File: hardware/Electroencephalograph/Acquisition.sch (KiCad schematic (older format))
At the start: 59 parts, among them U1 ADS1298IPAG, U2 OPA330xxD

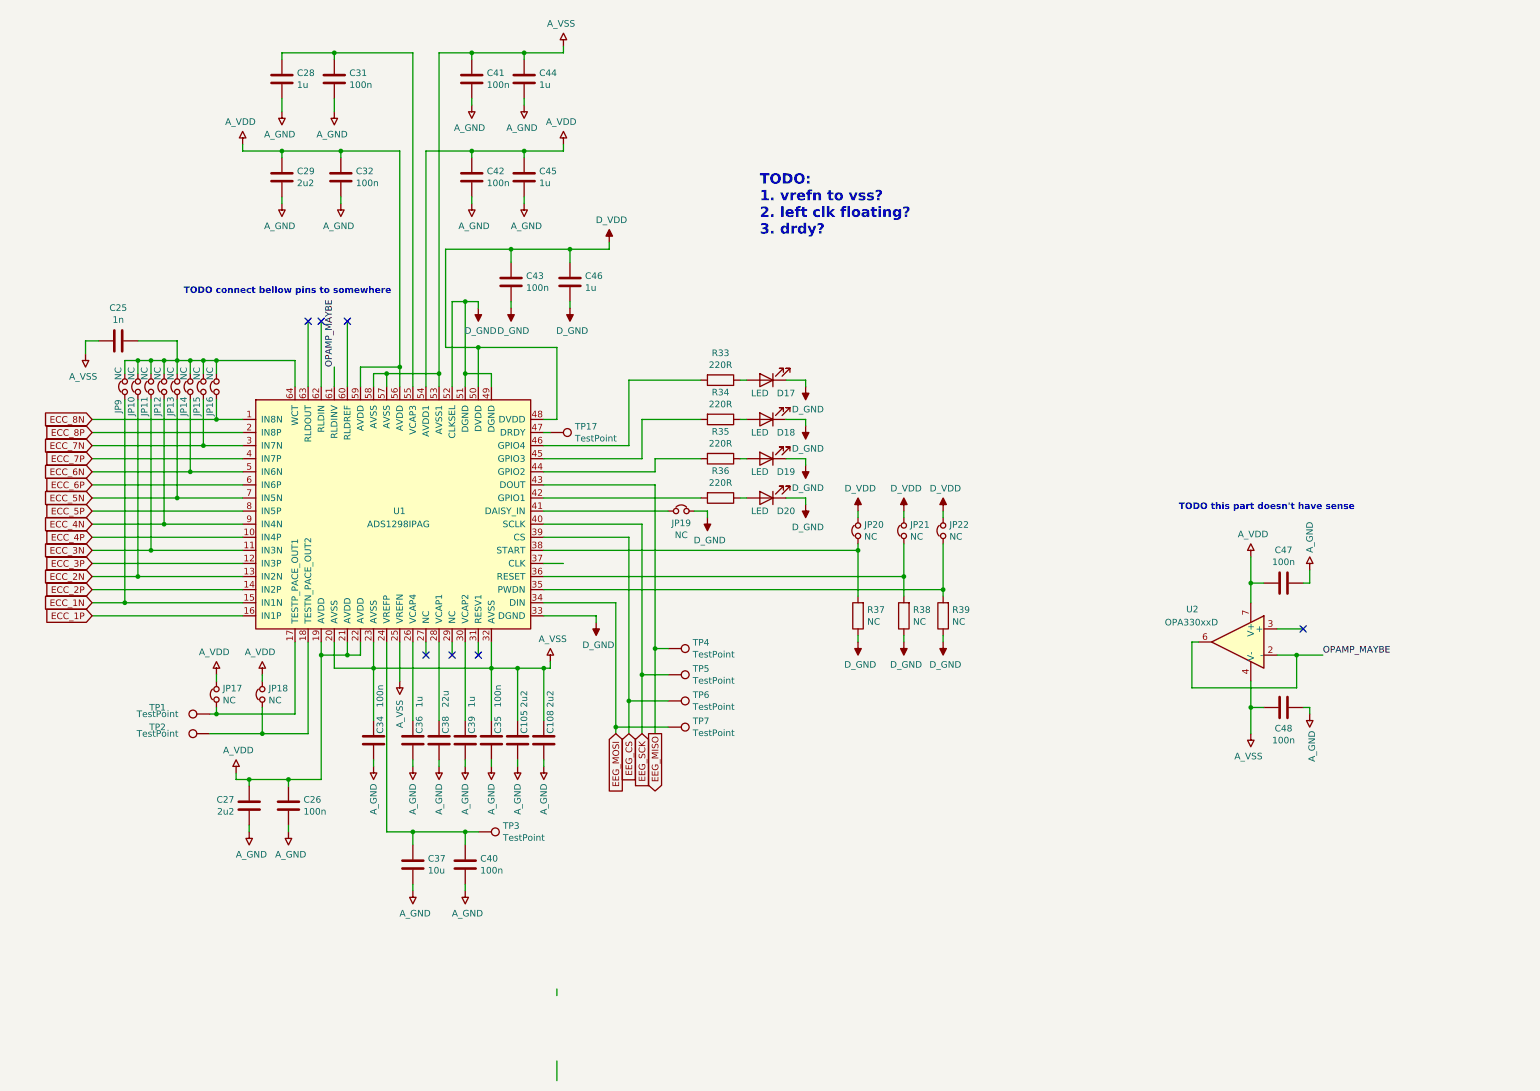
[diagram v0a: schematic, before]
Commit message: split user interface to separate sheets
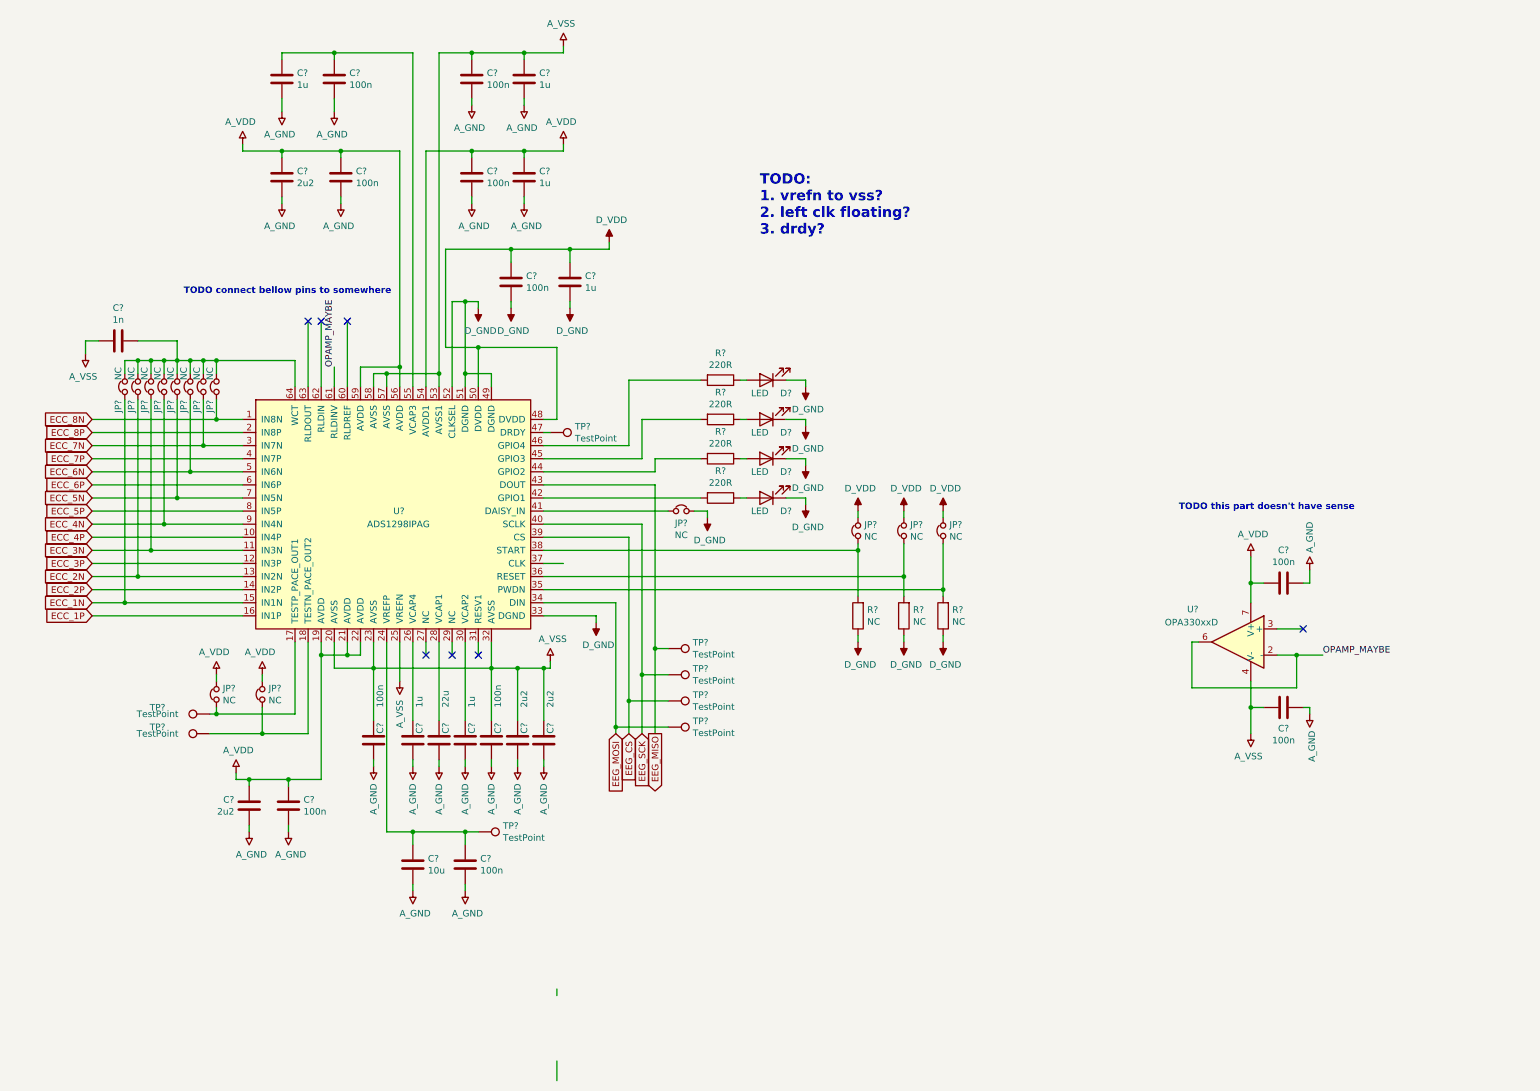
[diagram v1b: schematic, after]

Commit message: fix esp circuit
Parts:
- renumbered TP7 to TP17, TP17 to TP4, TP4 to TP5, TP5 to TP6, TP6 to TP7

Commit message: draft of mcu routing
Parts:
- D17, D18, D19, D20: footprint LED_SMD:LED_0603_1608Metric -> LED_SMD:LED_0402_1005Metric
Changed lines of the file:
@@
 F 0 "D20" H 6050 4300 50  0000 C CNN
 F 1 "LED" H 6250 4300 50  0000 C CNN
-F 2 "LED_SMD:LED_0603_1608Metric" H 6200 4200 50  0001 C CNN
+F 2 "LED_SMD:LED_0402_1005Metric" H 6200 4200 50  0001 C CNN
 F 3 "~" H 6200 4200 50  0001 C CNN
 	1    6200 4200
@@
 F 0 "D17" H 6050 3400 50  0000 C CNN
 F 1 "LED" H 6250 3400 50  0000 C CNN
-F 2 "LED_SMD:LED_0603_1608Metric" H 6200 3300 50  0001 C CNN
+F 2 "LED_SMD:LED_0402_1005Metric" H 6200 3300 50  0001 C CNN
 F 3 "~" H 6200 3300 50  0001 C CNN
 	1    6200 3300
@@
 F 0 "D18" H 6050 3700 50  0000 C CNN
 F 1 "LED" H 6250 3700 50  0000 C CNN
-F 2 "LED_SMD:LED_0603_1608Metric" H 6200 3600 50  0001 C CNN
+F 2 "LED_SMD:LED_0402_1005Metric" H 6200 3600 50  0001 C CNN
 F 3 "~" H 6200 3600 50  0001 C CNN
 	1    6200 3600
@@
 F 0 "D19" H 6050 4000 50  0000 C CNN
 F 1 "LED" H 6250 4000 50  0000 C CNN
-F 2 "LED_SMD:LED_0603_1608Metric" H 6200 3900 50  0001 C CNN
+F 2 "LED_SMD:LED_0402_1005Metric" H 6200 3900 50  0001 C CNN
 F 3 "~" H 6200 3900 50  0001 C CNN
 	1    6200 3900

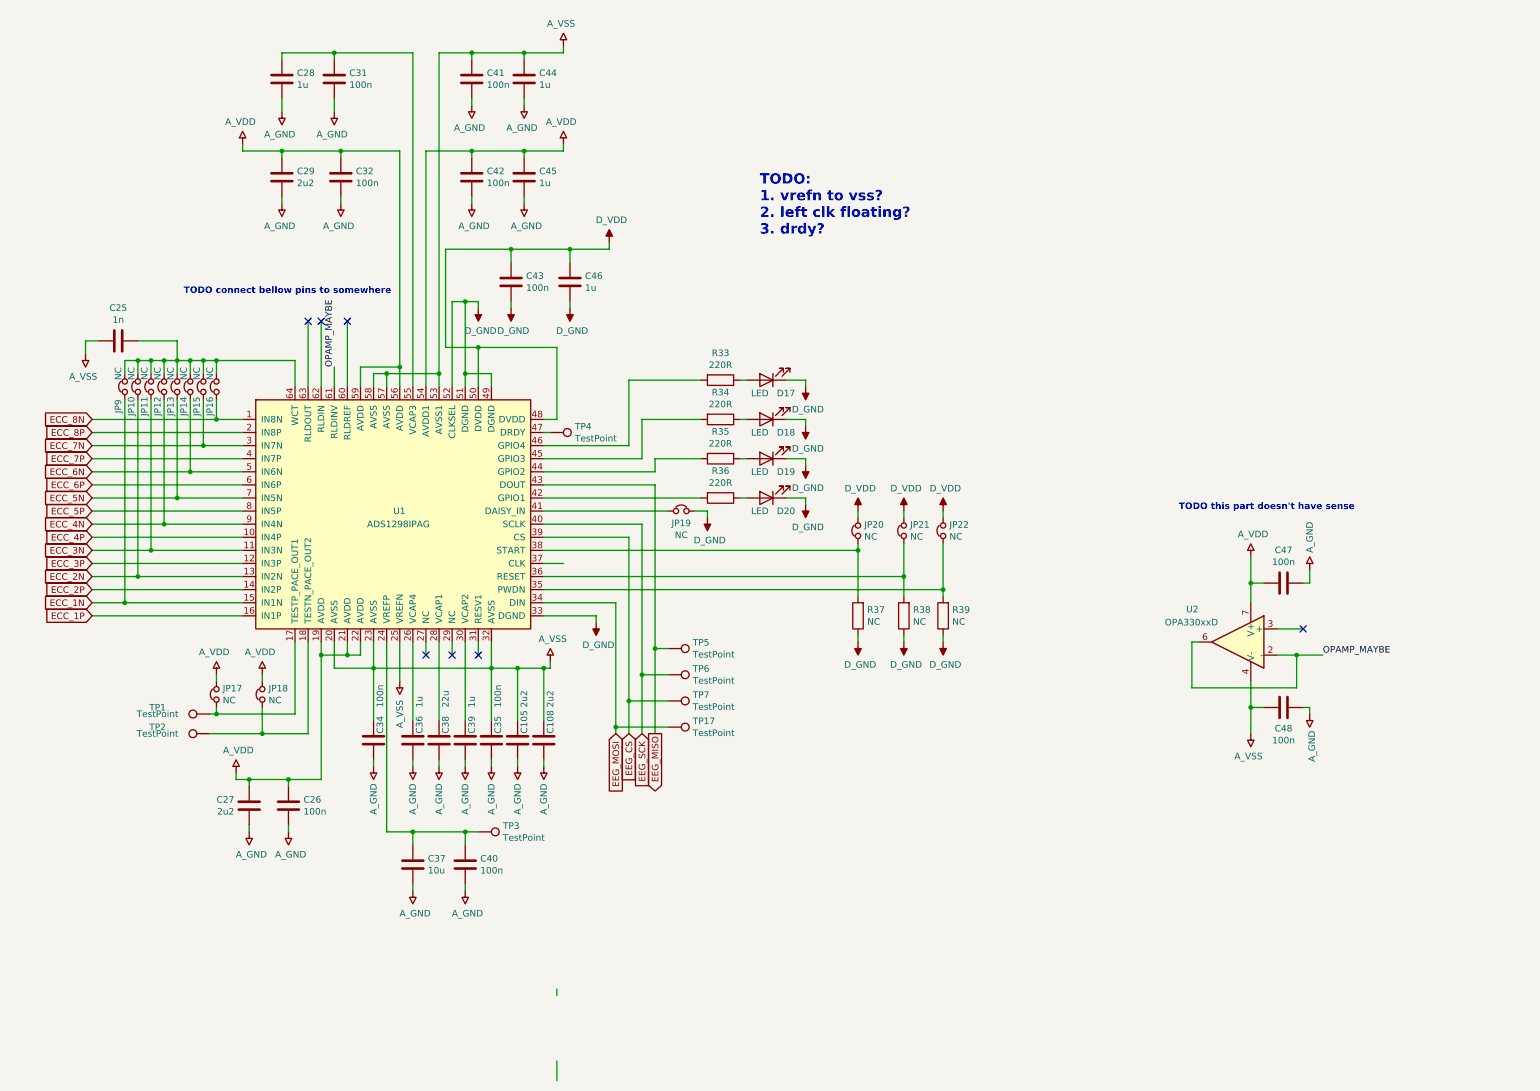
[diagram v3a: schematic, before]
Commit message: add right leg signal, update REDME
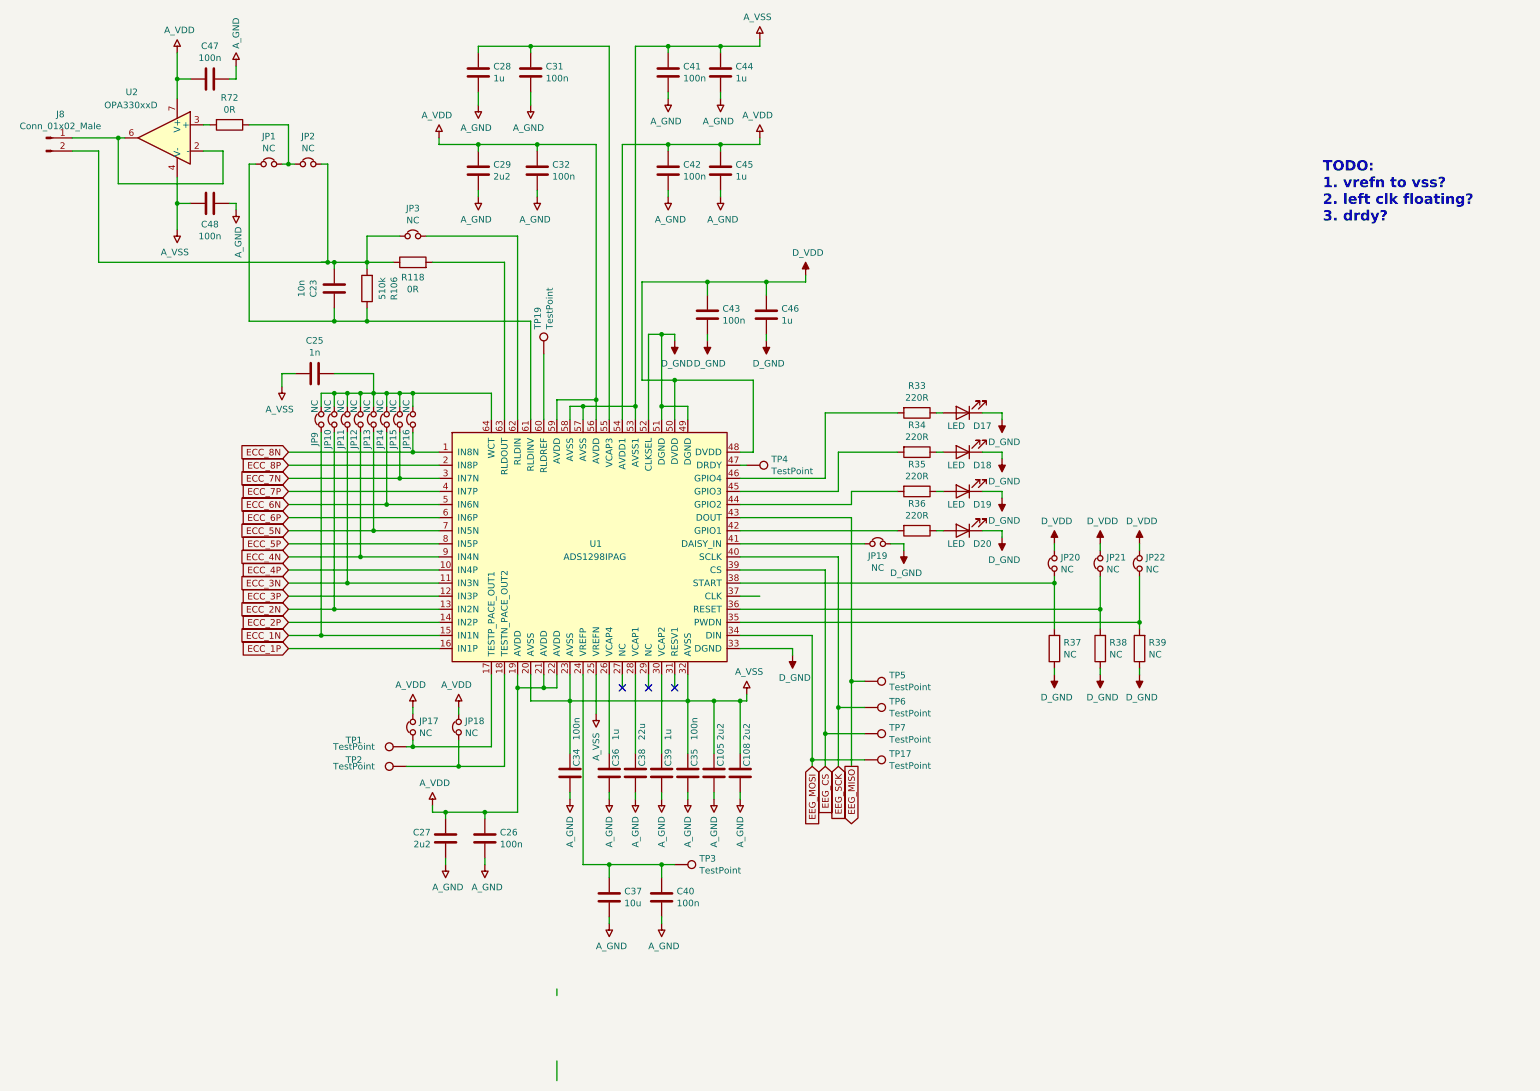
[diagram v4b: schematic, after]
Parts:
- added C23: 10n, Capacitor_SMD:C_0402_1005Metric, symbol Device:C
- added J8: Conn_01x02_Male, Connector_PinHeader_2.54mm:PinHeader_1x02_P2.54mm_Vertical, symbol Connector:Conn_01x02_Male
- added JP1, JP2, JP3: NC, Jumper:SolderJumper-2_P1.3mm_Bridged_Pad1.0x1.5mm, symbol Device:Jumper_NC_Small
- added R106: 510k, Resistor_SMD:R_0402_1005Metric, symbol Device:R
- added R118, R72: 0R, Resistor_SMD:R_0402_1005Metric, symbol Device:R
- added TP19: TestPoint, TestPoint:TestPoint_Pad_D1.0mm, symbol Connector:TestPoint
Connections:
- net at U1.60 (RLDREF): now also TP19.1
- net at U1.62 (RLDIN): now also JP3.1
- net at U1.63 (RLDOUT): now also R118.2
- net at U2.3 (+): now also R72.2
- net OPAMP_MAYBE: no longer names the net of U2.2 (-), U2.6
- net OPAMP_MAYBE: now also J8.1 (Pin_1); no longer U1.61 (RLDINV)
- new net: C23.2, JP1.2, R106.1, U1.61 (RLDINV)
- new net: JP1.1, JP2.2, R72.1
- new net: C23.1, J8.2 (Pin_2), JP2.1, JP3.2, R106.2, R118.1
- no-connect marks 7 -> 3
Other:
- note removed: "TODO connect bellow pins to somewhere"
- note removed: "TODO this part doesn't have sense"
- moved on the sheet: C105, C108, C25, C26, C27, C28, C29, C31, C32, C34, C35, C36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
